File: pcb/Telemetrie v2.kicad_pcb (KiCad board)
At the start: 4 copper layers, 100 x 91 mm, 68 parts, among them J1 Conn_02x03_Odd_Even, J2 Conn_01x02_Pin, J3 CONSMA001-SMD-G-T, J4 Conn_01x04_Pin, J5 Conn_01x02_Pin, M1 Conn_01x01_Pin, M2 Conn_01x01_Pin, M3 Conn_01x01_Pin, M4 Conn_01x01_Pin, U1 AVR128DB64x-xPT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

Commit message: update pcb
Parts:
- added D13: LED, LED_SMD:LED_0805_2012Metric_Pad1.15x1.40mm_HandSolder, F.Cu at (-12.5, -32.1)
- added D14: LED, LED_SMD:LED_0805_2012Metric_Pad1.15x1.40mm_HandSolder, F.Cu at (-16.0, -37.1)
- added D15: LED, LED_SMD:LED_0805_2012Metric_Pad1.15x1.40mm_HandSolder, F.Cu at (-21.6, 8.88)
- added D16: LED, LED_SMD:LED_0805_2012Metric_Pad1.15x1.40mm_HandSolder, F.Cu at (-17.0, 8.88)
- added R13: 100R, Resistor_SMD:R_0805_2012Metric_Pad1.20x1.40mm_HandSolder, F.Cu at (-12.5, -27.1)
- added R14: 100R, Resistor_SMD:R_0805_2012Metric_Pad1.20x1.40mm_HandSolder, F.Cu at (-16.0, -32.1)
- added R15: 100R, Resistor_SMD:R_0805_2012Metric_Pad1.20x1.40mm_HandSolder, F.Cu at (-21.6, 12.9)
- added R16: 100R, Resistor_SMD:R_0805_2012Metric_Pad1.20x1.40mm_HandSolder, F.Cu at (-17.0, 12.9)
- moved R19 4.34 mm to (-12.5, -22.1)
- moved TP9 2.38 mm to (-17.0, 18.4)
- moved TP3 2.12 mm to (-10.5, -37.9)
- moved TP4 2.12 mm to (-13.0, -40.4)
- moved TP1 2.00 mm to (-15.7, 4.00)
- moved TP7 1.88 mm to (-14.4, 21.9)
- moved TP8 1.88 mm to (-19.5, 21.9)
- renumbered R15 to R17, R16 to R18, R13 to R19, R14 to R20
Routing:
- net +3V3: track 45.4 -> 57.8 mm, vias 8 -> 14
- net RX4: track 34.1 -> 38.6 mm
- net TXD: track 39.1 -> 43.0 mm
- net RXD: track 36.7 -> 40.6 mm
- net Net-(D14-K): track 0.00 -> 2.98 mm
- net Net-(D13-K): track 0.00 -> 2.98 mm
- net TX4: track 33.2 -> 36.1 mm
- net RST: track 69.0 -> 67.0 mm
- net +5V: track 108.6 -> 110.6 mm, vias 1 -> 3
- net Net-(D16-K): track 0.00 -> 1.97 mm
- net Net-(D15-K): track 0.00 -> 1.97 mm
- net Net-(U2-RESET): track 24.2 -> 23.1 mm

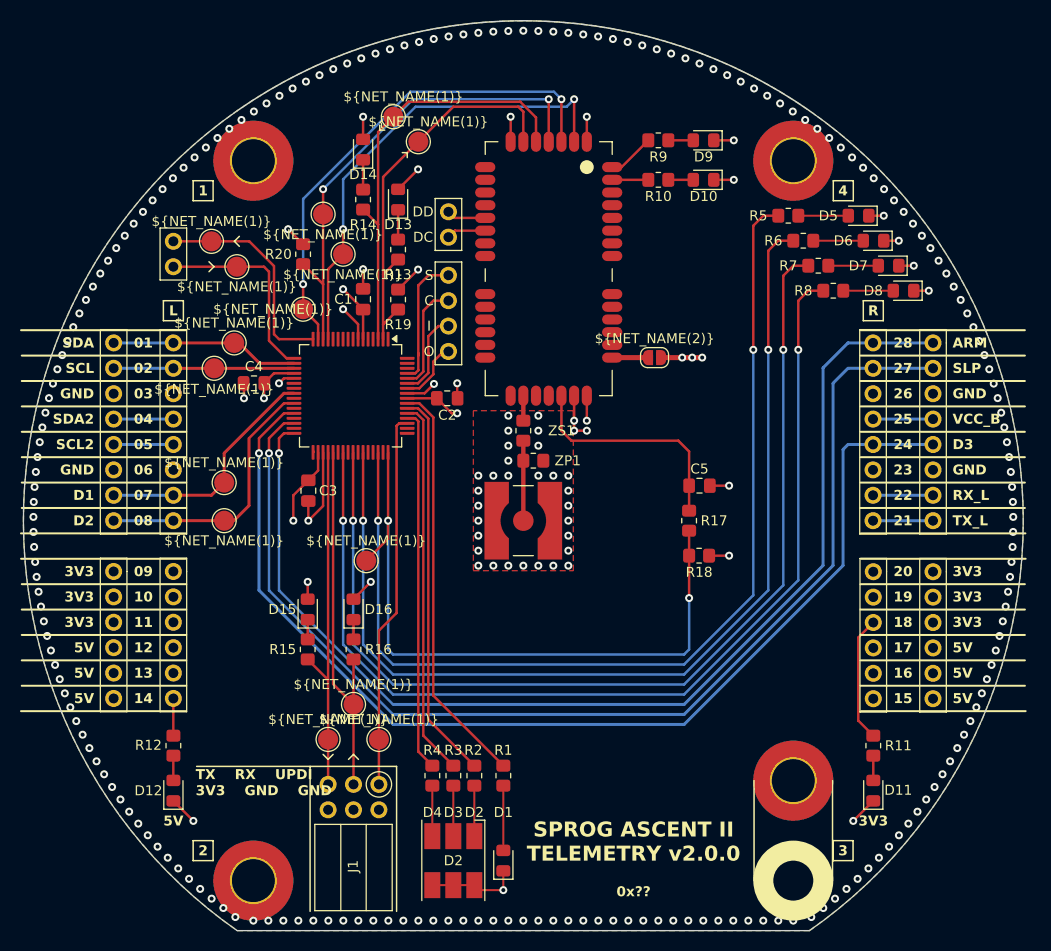
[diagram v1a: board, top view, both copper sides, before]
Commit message: silkscreen and schematic update
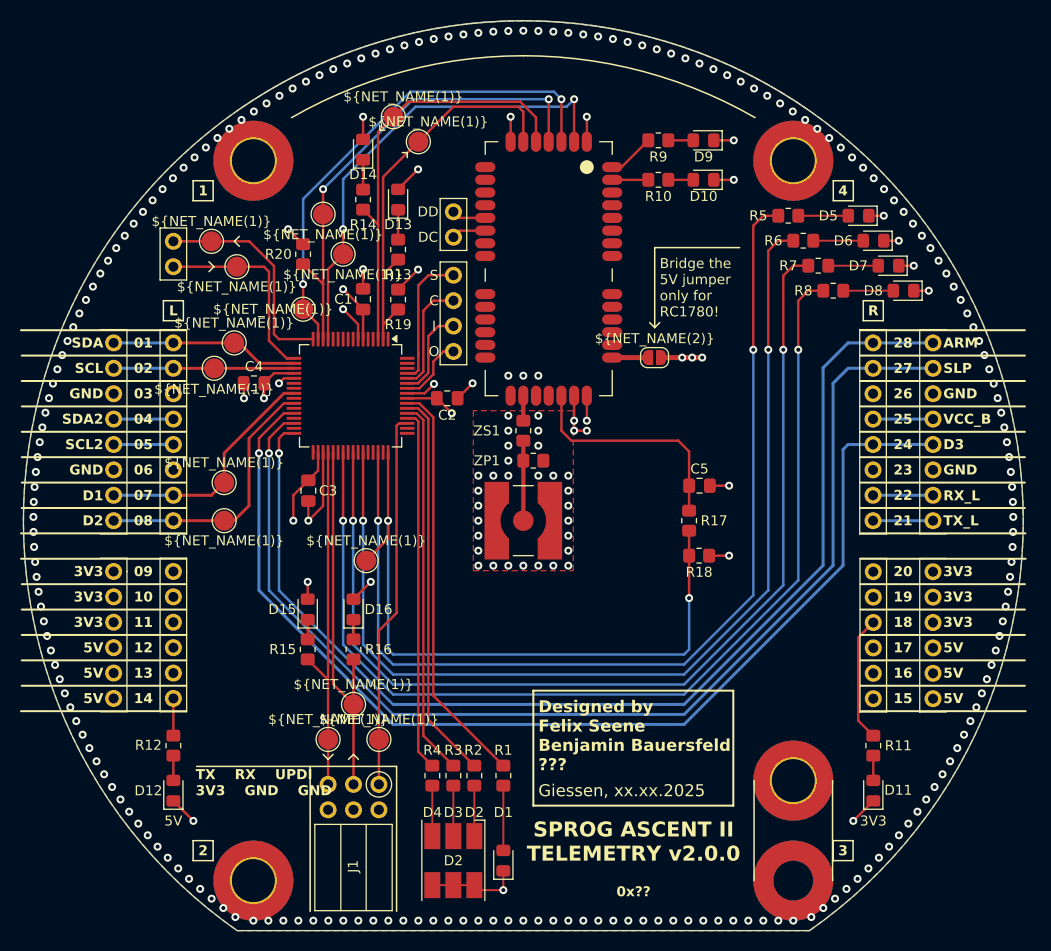
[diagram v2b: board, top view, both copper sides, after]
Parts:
- moved J2 0.50 mm to (-6.99, -30.9)
- moved J4 0.50 mm to (-6.99, -16.9)
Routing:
- net GND: track 55.1 -> 55.8 mm, vias 252 -> 255
- net +3V3: track 57.8 -> 57.2 mm
- net SS: track 13.4 -> 13.9 mm
- net SCK: track 10.9 -> 11.4 mm
- net Net-(J2-Pin_2): track 3.95 -> 3.45 mm
- net Net-(J2-Pin_1): track 3.93 -> 3.43 mm
- net MISO: track 8.92 -> 9.42 mm
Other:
- board text added: "Bridge the 5V jumper only for RC1780!"
- board text added: "Designed by Felix Seene Benjamin Bauersfeld ???"
- board text added: "Giessen, xx.xx.2025"

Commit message: update schematic and silkscreen
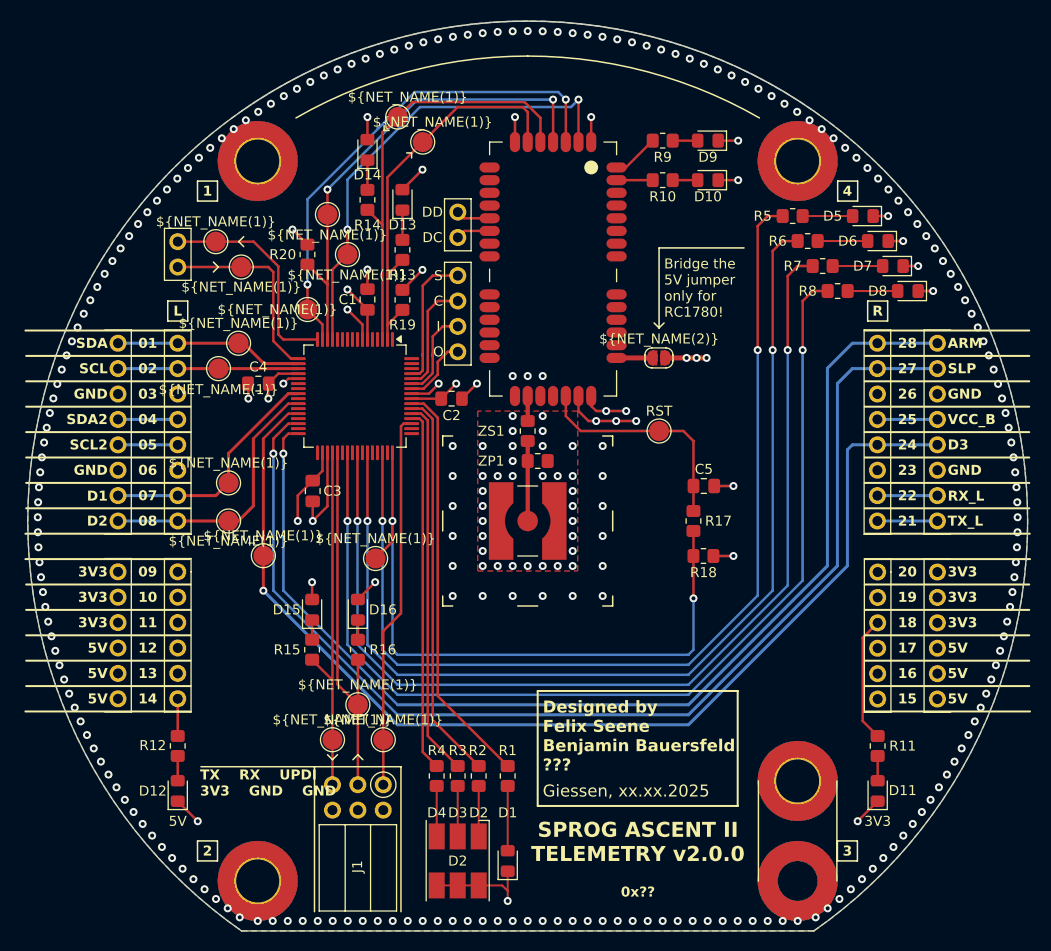
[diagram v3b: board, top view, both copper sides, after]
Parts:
- added TP16: ~, Footprints:TestPoint, F.Cu at (13.6, -8.97)
- added TP17: ~, Footprints:TestPoint, F.Cu at (-26.0, 3.50)
- J3: value CONSMA001-SMD-G-T -> SMA SMD
- moved TP1 0.96 mm to (-14.8, 3.78)
- moved JR1 0.44 mm to (35.4, -17.7)
- moved JR3 0.44 mm to (41.4, -17.7)
- moved JR4 0.44 mm to (41.4, 5.14)
- moved JP1 0.44 mm to (13.6, -16.3)
- moved C3 0.44 mm to (-21.1, -2.97)
- moved C4 0.44 mm to (-26.5, -13.7)
- moved C5 0.44 mm to (18.1, -3.47)
- moved D16 0.44 mm to (-16.5, 8.91)
- moved R16 0.44 mm to (-16.5, 12.9)
- moved U1 0.44 mm to (-16.8, -12.5)
- moved J1 0.44 mm to (-19.1, 26.4)
- moved M1 0.44 mm to (-26.6, -36.0)
- moved M2 0.44 mm to (-26.6, 36.0)
- moved M3 0.44 mm to (27.4, 26.0)
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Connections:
- net RXD renamed TX0
- net TXD renamed RX0
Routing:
- net GND: track 55.8 -> 59.1 mm, vias 255 -> 274
- net +3V3: track 57.2 -> 60.2 mm

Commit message: pcb update
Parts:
- moved JR1 0.44 mm to (35.0, -17.8)
- moved JR3 0.44 mm to (41.0, -17.8)
- moved JR4 0.44 mm to (41.0, 5.10)
- moved R10 0.44 mm to (13.5, -34.1)
- moved C2 0.44 mm to (-7.61, -12.2)
- moved C3 0.44 mm to (-21.5, -3.00)
- moved C4 0.44 mm to (-26.9, -13.7)
- moved C5 0.44 mm to (17.6, -3.50)
- moved D15 0.44 mm to (-21.6, 8.87)
- moved D16 0.44 mm to (-17.0, 8.87)
- moved JP1 0.44 mm to (13.1, -16.3)
- moved R13 0.44 mm to (-12.5, -27.1)
- moved R15 0.44 mm to (-21.6, 12.9)
- moved R16 0.44 mm to (-17.0, 12.9)
- moved R19 0.44 mm to (-12.5, -22.1)
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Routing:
- net GND: track 59.1 -> 61.1 mm, vias 274 -> 294

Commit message: update pcb
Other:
- board text added: "Designed by Felix Seene Benjamin Bauersfeld"
- board text added: "Giessen, 18.07.2025"
- board text removed: "Designed by Felix Seene Benjamin Bauersfeld ???"
- board text removed: "Giessen, xx.xx.2025"
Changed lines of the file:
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@@
 		)
 	)
-	(gr_text "Designed by\nFelix Seene\nBenjamin Bauersfeld\n???"
+	(gr_text "Designed by\nFelix Seene\nBenjamin Bauersfeld"
 		(at 1.500011 21.49996 0)
 		(layer "F.SilkS")
@@
 		)
 	)
-	(gr_text "Giessen, xx.xx.2025"
+	(gr_text "Giessen, 18.07.2025"
 		(at 1.500011 26.99996 0)
 		(layer "F.SilkS")
